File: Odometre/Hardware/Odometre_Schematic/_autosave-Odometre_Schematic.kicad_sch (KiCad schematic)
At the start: 28 parts, among them IC1 STM32C092FCP6, J1 Conn_01x03_Pin, J2 Conn_01x03_Pin, J3 Conn_Alim, J4 Conn_Laser1, J5 Conn_Laser2, J6 Conn_01x06_Pin, J7 Conn_01x06_Pin, SW1 SW_Push, U1 MCP2562-E-SN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

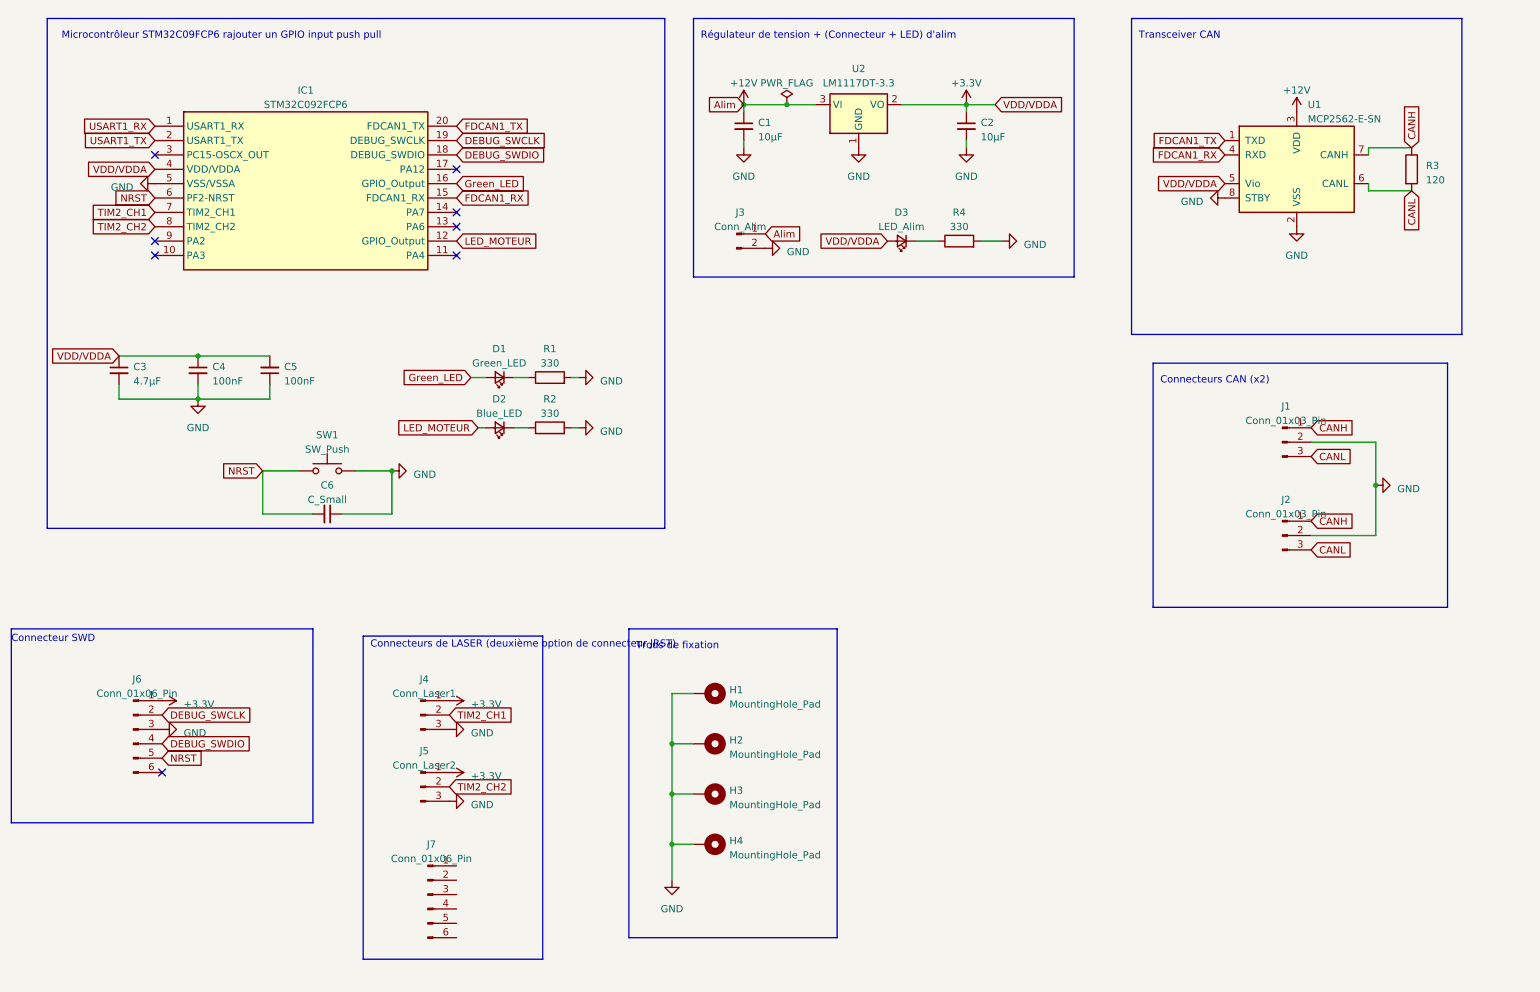
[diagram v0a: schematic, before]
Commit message: modification d'une pin dans l'ioc
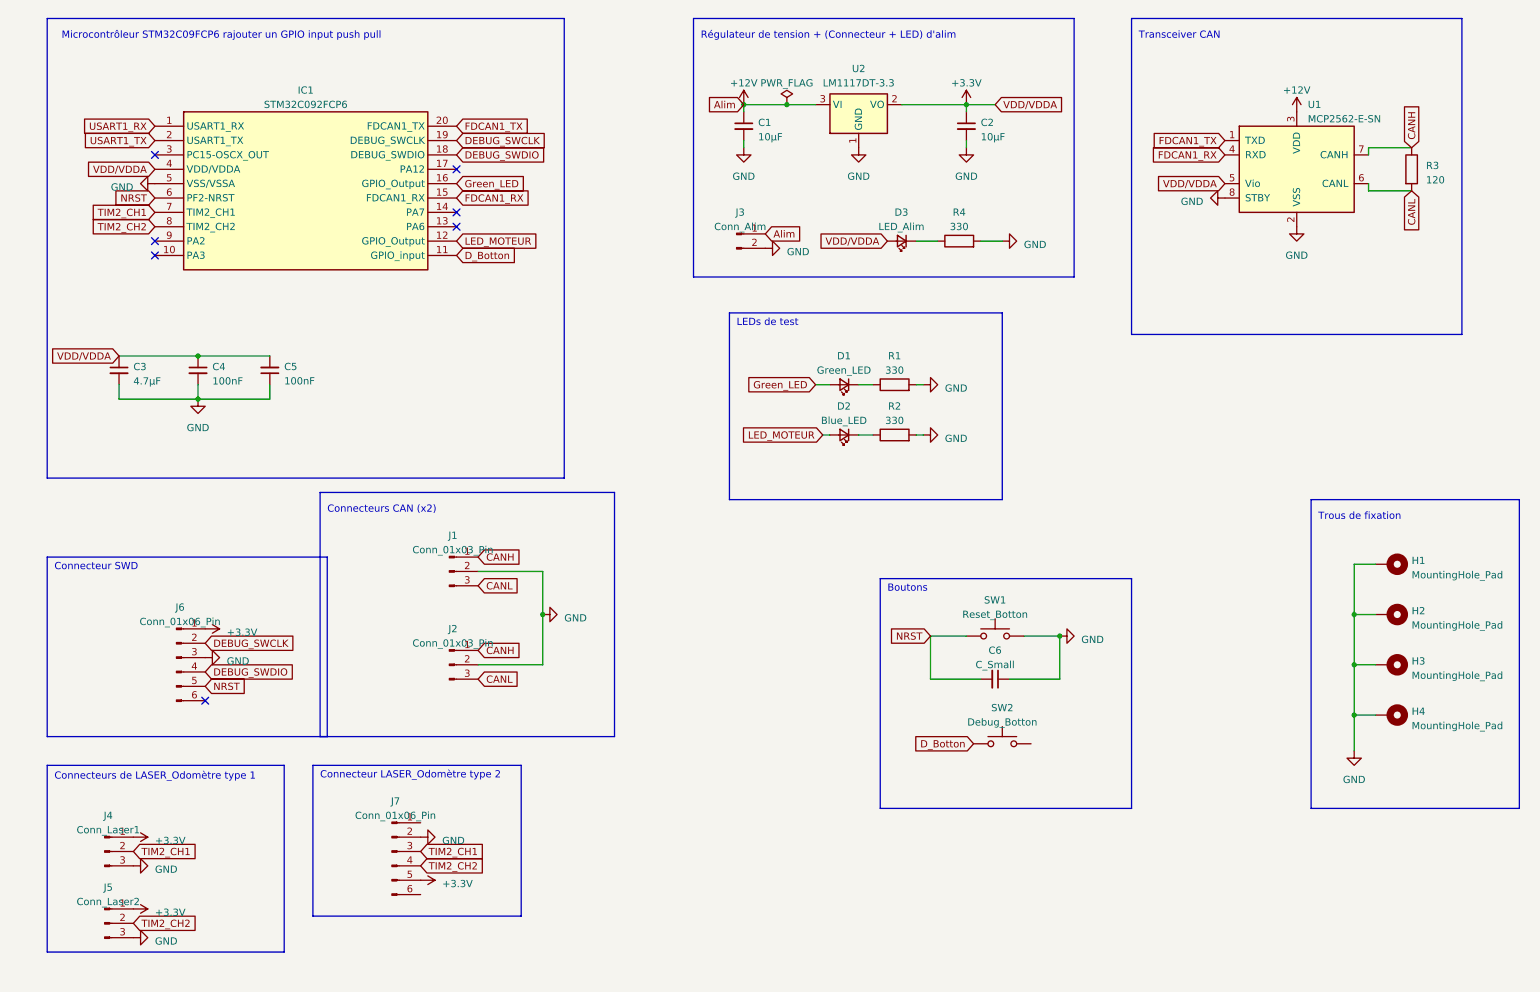
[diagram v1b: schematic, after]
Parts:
- added SW2: Debug_Botton, Button_Switch_THT:SW_PUSH_6mm, symbol Switch:SW_Push
- SW1: value SW_Push -> Reset_Botton
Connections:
- net +3.3V: now also J7.5 (Pin_5)
- net GND: now also J7.2 (Pin_2)
- net TIM2_CH1: now also J7.3 (Pin_3)
- net TIM2_CH2: now also J7.4 (Pin_4)
- net D_Botton: now reaches IC1.11 (GPIO_input)
- net D_Botton: now also SW2.1
- no-connect marks 8 -> 7
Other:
- note added: "Boutons"
- note added: "Connecteur LASER_Odomètre type 2"
- note added: "Connecteurs de LASER_Odomètre type 1"
- note added: "LEDs de test"
- note removed: "Connecteurs de LASER (deuxième option de connecteur JRST)"
- moved on the sheet: C6, D1, D2, H1, H2, H3, H4, J1, J2, J4, J5, J6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

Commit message: modif ioc
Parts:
- added C7: 100nF, symbol Device:C_Small
- added C8, C9: 10µF, Capacitor_SMD:C_0805_2012Metric_Pad1.18x1.45mm_HandSolder, symbol Device:C_Small
- added D4: LED_Trans, symbol Device:LED_Small
- added R5: 330, symbol Device:R
- added U3: LM1117DT-5.0, Package_TO_SOT_SMD:TO-252-3_TabPin2, symbol Regulator_Linear:LM1117DT-5.0
- R2: value 330 -> 100
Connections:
- net +12V: now also C8.1, C9.1, D4.2 (A), U3.2 (VO), U3.3 (VI)
- net +3.3V: now also C7.1
- net GND: now also SW2.2, C7.2, C8.2, C9.2, R5.2, U3.1 (GND)
- net USART1_RX: no longer names the net of IC1.1 (PB7)
- net USART1_TX: no longer names the net of IC1.2 (PC14)
- new net: D4.1 (K), R5.1
- no-connect marks 7 -> 11
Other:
- moved on the sheet: C1, C2, C3, C4, C5, C6, D1, D2, D3, H1, H2, H3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
